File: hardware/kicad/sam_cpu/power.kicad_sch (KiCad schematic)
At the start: 29 parts, among them J11 J11 POWER, J17 EXT 5V, Q1 AO3401A, Q2 AO3401A, U1 LTC4412, U2 LTC4412, U3 AMS1117-3.3

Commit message: Redraw the schematic with wires (draft 0.2)
Every connection is now a wire, and each connector sits on the page of the
parts that drive or read it (Pi header with the RP2354B, J6/J12 with their
comparators and 74HC165, J1 with the 74HC595, J2/J3/J13 with their filters).
Signals between pages use global labels with page references. The Pi page is
merged into the MCU page; the Pi 4 sits on the 40-pin header J21.

ERC: 0 errors, 1 warning. Netlist check: 1266 pins, 299 nets, no differences.

Co-Authored-By: Claude Opus 5.5 (1M context) <noreply@anthropic.com>
Claude-Session: https://claude.ai/code/session_019DLTv1F2PjepjxqiUcAMKV
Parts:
- added C10: 100n, Capacitor_SMD:C_0603_1608Metric, symbol Device:C
- added D4: S1M, Diode_SMD:D_SMA, symbol Device:D
- C1: value 47u -> 100u; footprint Capacitor_SMD:CP_Elec_6.3x7.7 -> Capacitor_SMD:CP_Elec_8x10
- C3: value 100u -> 47u; footprint Capacitor_SMD:CP_Elec_8x10 -> Capacitor_SMD:CP_Elec_6.3x7.7
- C4: footprint Capacitor_SMD:CP_Elec_8x10 -> Capacitor_SMD:CP_Elec_6.3x7.7
- C8: value 100n -> 100u; footprint Capacitor_SMD:C_0603_1608Metric -> Capacitor_SMD:CP_Elec_6.3x7.7; symbol Device:C -> Device:C_Polarized
- FB1: value FB 3A -> 3A
- FB2, FB3: value FB 1A -> 1A
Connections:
- net +12V: now also C2.1; no longer C1.1
- net +5V: now also D4.2 (A)
- net -12V: now also C3.2; no longer C2.2
- net GND: now also C2.2, C3.1, C10.2; no longer C2.1, C3.2
- net VMON_12V: now also C10.1; no longer C9.1
- net VMON_5V: now also C9.1; no longer C8.1
- net +12V_IN: no longer names the net of FB2.1, J11.6 (Pin_6)
- net +5V_EXT: no longer names the net of D1.1 (A1), J17.1 (Pin_1), Q1.3 (D), R1.1, U1.1 (VIN)
- net +5V_EXT: now also C1.1; no longer C3.1
- net +5V_J11: no longer names the net of JP1.2 (B), Q2.3 (D), U2.1 (VIN)
- net +5V_J11_F: no longer names the net of FB1.2, JP1.1 (A)
- net +5V_J11_IN: no longer names the net of FB1.1, J11.1 (Pin_1)
- net -12V_IN: no longer names the net of FB3.1, J11.3 (Pin_3)
- net EXT_PRESENT: no longer names the net of R1.2, R2.1, U2.3 (CTL)
- net GATE_EXT: no longer names the net of Q1.1 (G), U1.5 (GATE)
- net GATE_J11: no longer names the net of Q2.1 (G), U2.5 (GATE)
- new net +4V5: C8.1, D4.1 (K)
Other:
- note added: "3.3 V"
- note added: "4.5 V for the switch matrix"
- note added: "External +5 V (J17, priority)"
- note added: "IO board power (J11)"
- note removed: "3.3 V regulator"
- note removed: "Ideal-diode power mux"
- note removed: "J11: power from the IO board (J16 harness)"
- note removed: "J17: external +5 V (priority)"
- title: Power: +5 V mux (external / J11), 3.3 V, supply monitors -> Power: +5 V mux (external / J11), 3.3 V, 4.5 V, supply monitors
- moved on the sheet: C1, C2, C3, C4, C5, C6, C7, C9, D1, D2, FB1, FB2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

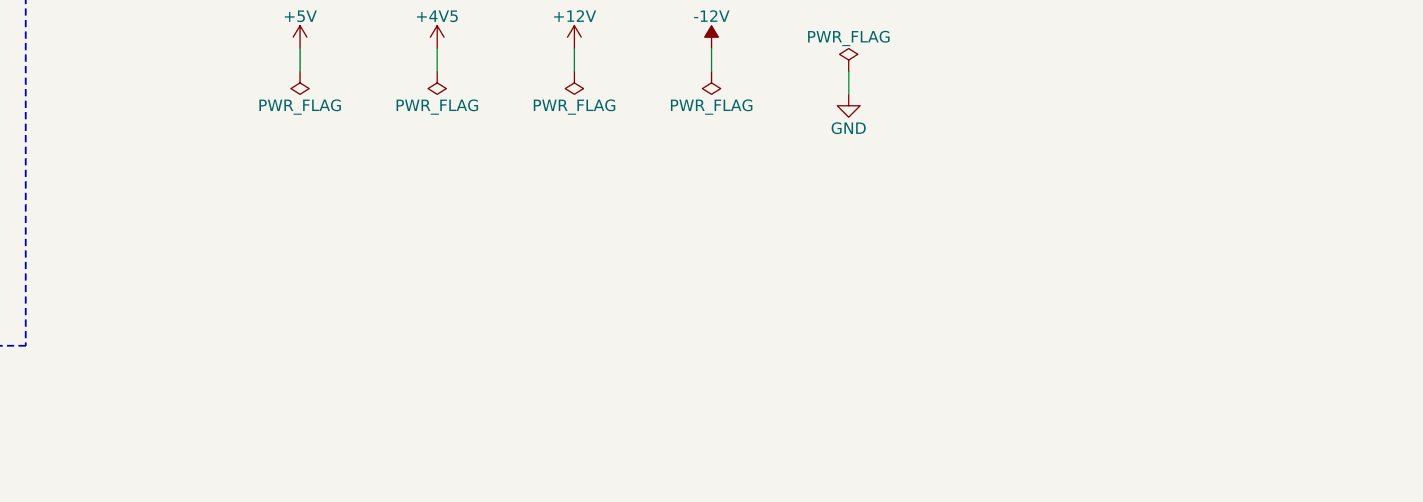
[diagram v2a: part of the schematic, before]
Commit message: Add RTC, test points and stereo speaker connector; place all parts on 2 layers
Schematic: DS3231MZ real-time clock on the Pi I2C1 with a CR2032 holder,
22 test points (rails, bus, strobes, switch chain, VREF, DAC outputs) and
J22, a second KK-396 speaker connector with L and R as separate pairs.
ERC 0 errors, generated netlist matches the intended nets.

PCB: 2 copper layers. The RP2354B sits near J9 with its USB-C on the top
edge 13 mm from the USB pins; decoupling, regulator and crystal parts on
their pins; every other part grouped by sheet next to its connector, low
parts only under the Pi. J17 and J22 on the right edge; Pi and J5 12 mm
lower to fit the audio parts.

Co-Authored-By: Claude Opus 5.5 (1M context) <noreply@anthropic.com>
Claude-Session: https://claude.ai/code/session_01ExuDVoDDDHhVWjb8EwVzYb
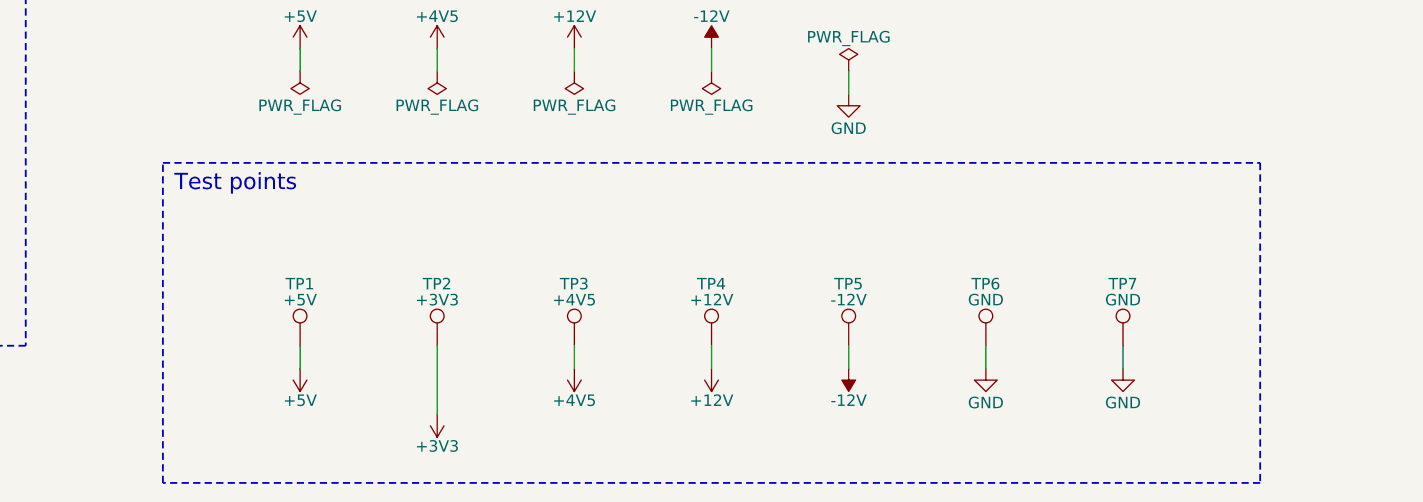
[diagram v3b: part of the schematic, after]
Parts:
- added TP1: +5V, TestPoint:TestPoint_Pad_D1.5mm, symbol Connector:TestPoint
- added TP2: +3V3, TestPoint:TestPoint_Pad_D1.5mm, symbol Connector:TestPoint
- added TP3: +4V5, TestPoint:TestPoint_Pad_D1.5mm, symbol Connector:TestPoint
- added TP4: +12V, TestPoint:TestPoint_Pad_D1.5mm, symbol Connector:TestPoint
- added TP5: -12V, TestPoint:TestPoint_Pad_D1.5mm, symbol Connector:TestPoint
- added TP6, TP7: GND, TestPoint:TestPoint_Pad_D1.5mm, symbol Connector:TestPoint
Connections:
- net +12V: now also TP4.1
- net +3V3: now also TP2.1
- net +4V5: now also TP3.1
- net +5V: now also TP1.1
- net -12V: now also TP5.1
- net GND: now also TP6.1, TP7.1
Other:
- note added: "Test points"

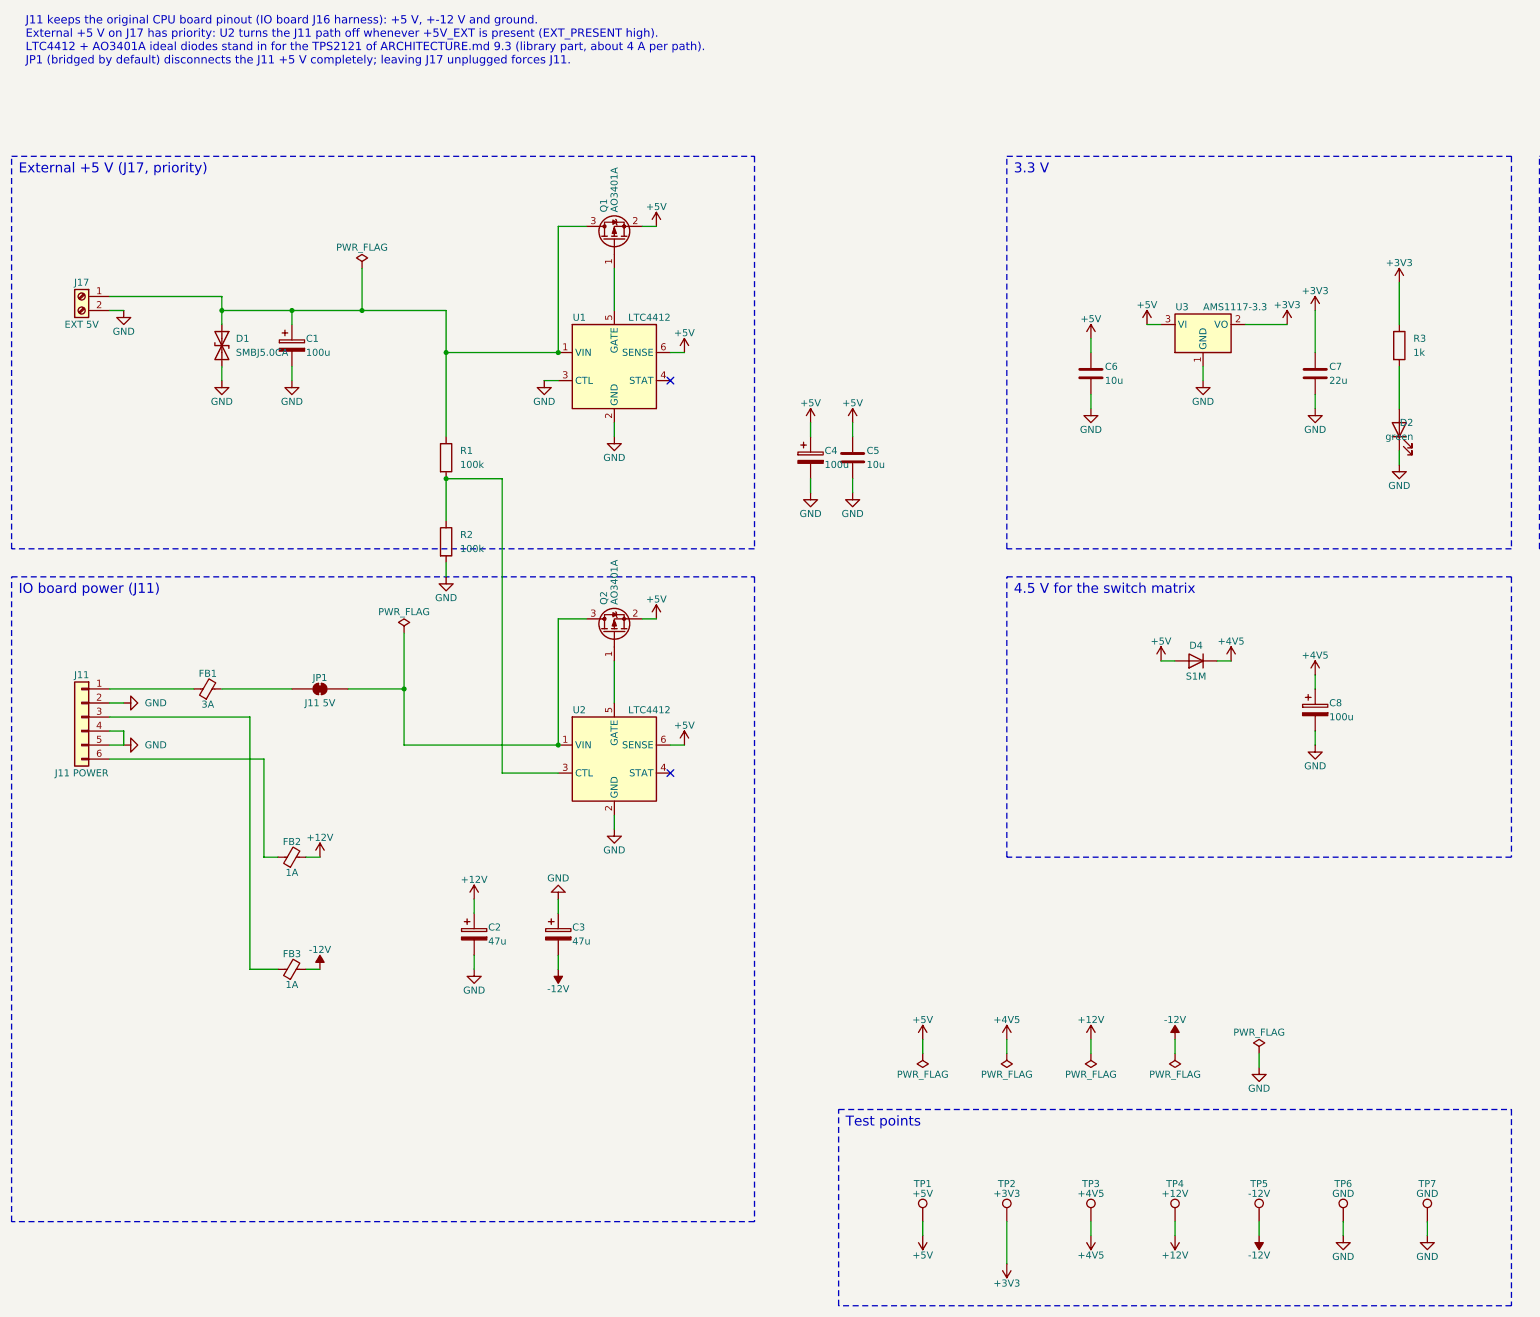
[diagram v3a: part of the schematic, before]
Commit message: Audio on external 12 V with TDA7297 stereo + subwoofer amps, NCP1117, guide regulator layout
- Remove the +-12 V input from J11; J23 external +12 V with polyfuse and TVS
- Replace the two TDA2030A with a TDA7297 bridge amp for left/right (J10, J22)
  and a second TDA7297 for the subwoofer (J24), fed by an (L+R)/2 110 Hz
  Sallen-Key low-pass (OPA1678); shared standby and RP2354B-controlled mute
- AMS1117 -> NCP1117-3.3 (ceramic-stable, as in the RP2350 guide), 10 uF 1206
- L1 and crystal part numbers from the RP2350 hardware guide
- Place the core regulator parts by hand following the Pico 2 layout; amps in a
  row with a heatsink keep-out; J23/J22/J24 on the right edge

Co-Authored-By: Claude Opus 5.5 (1M context) <noreply@anthropic.com>
Claude-Session: https://claude.ai/code/session_01ExuDVoDDDHhVWjb8EwVzYb
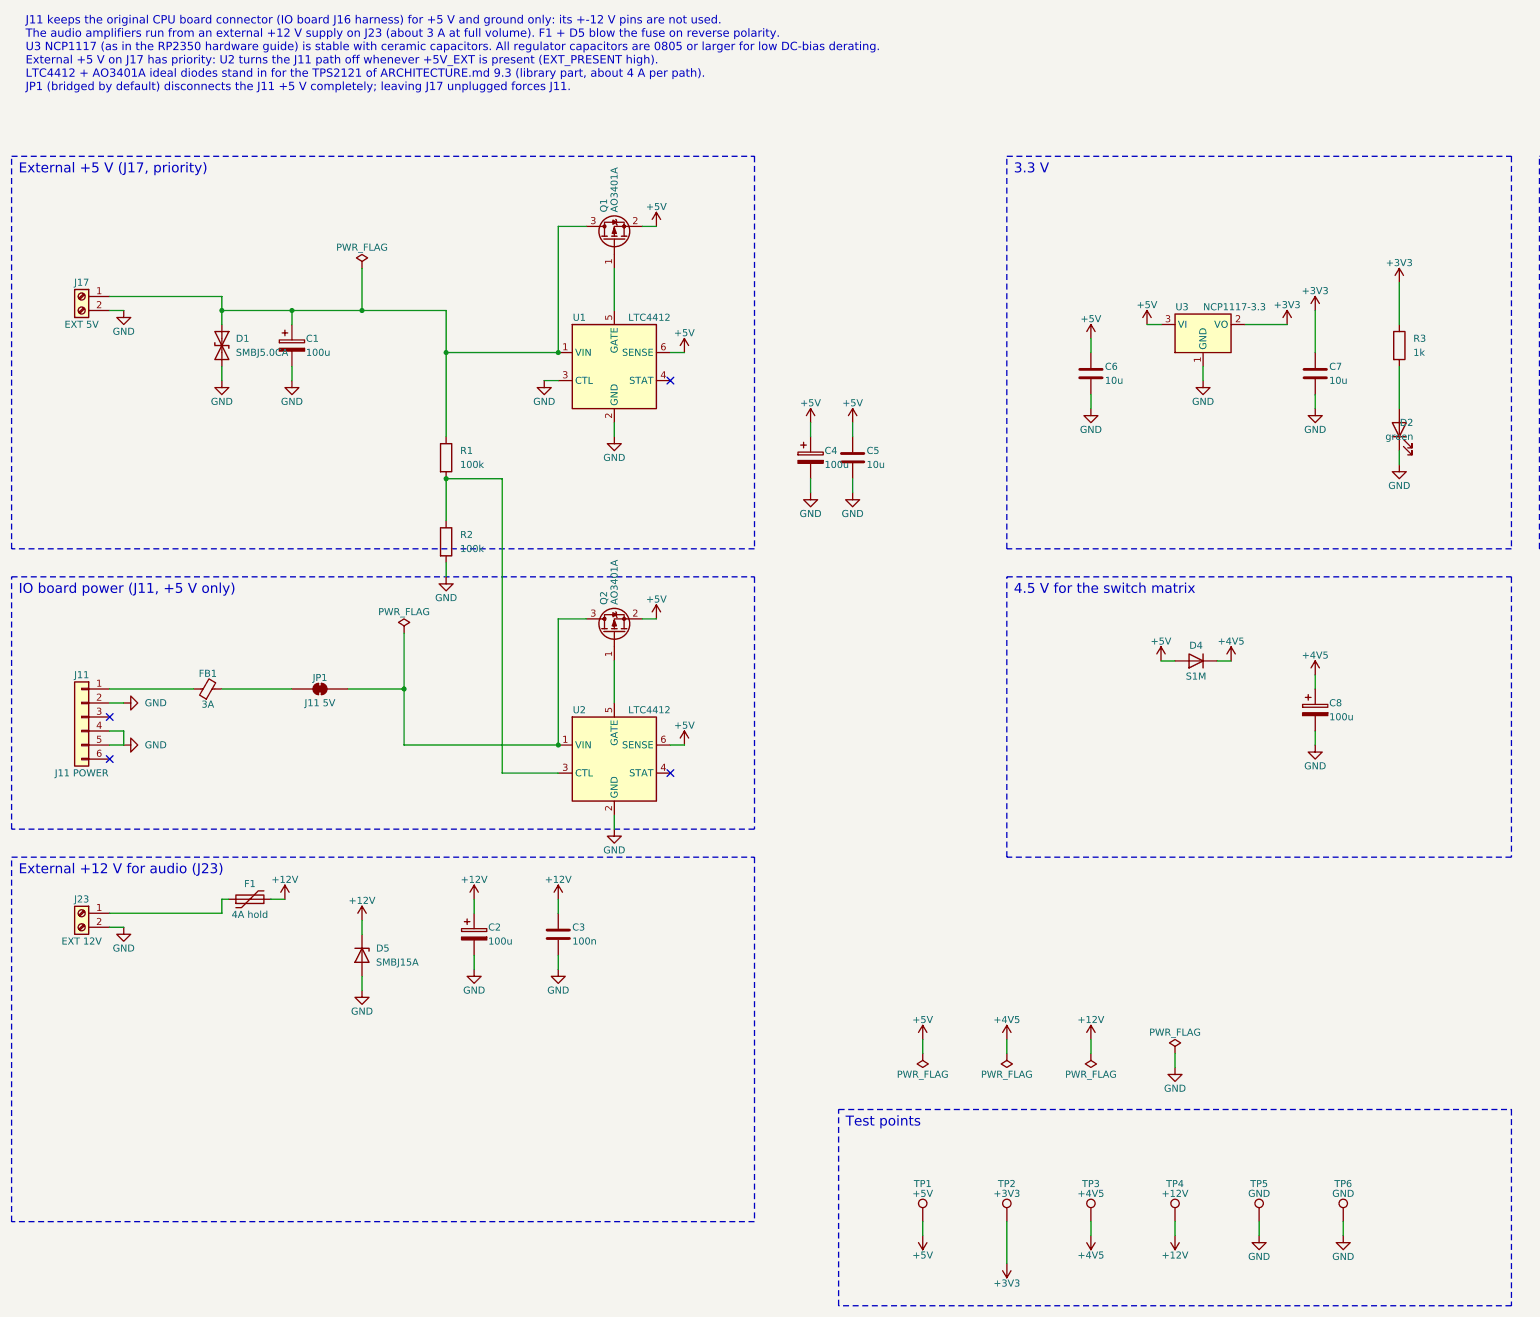
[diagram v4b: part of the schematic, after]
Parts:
- removed FB2, FB3: 1A, Inductor_SMD:L_0805_2012Metric, symbol Device:FerriteBead_Small
- removed TP7: GND, TestPoint:TestPoint_Pad_D1.5mm, symbol Connector:TestPoint
- added D5: SMBJ15A, Diode_SMD:D_SMB, symbol Device:D_Zener
- added F1: 4A hold, Fuse:Fuse_2920_7451Metric, symbol Device:Polyfuse
- added J23: EXT 12V, TerminalBlock_Phoenix:TerminalBlock_Phoenix_MKDS-1,5-2-5.08_1x02_P5.08mm_Horizontal, symbol Connector:Screw_Terminal_01x02
- C2: value 47u -> 100u; footprint Capacitor_SMD:CP_Elec_6.3x7.7 -> Capacitor_SMD:CP_Elec_8x10
- C3: value 47u -> 100n; footprint Capacitor_SMD:CP_Elec_6.3x7.7 -> Capacitor_SMD:C_0603_1608Metric; symbol Device:C_Polarized -> Device:C
- C6: footprint Capacitor_SMD:C_0805_2012Metric -> Capacitor_SMD:C_1206_3216Metric
- C7: value 22u -> 10u; footprint Capacitor_SMD:C_0805_2012Metric -> Capacitor_SMD:C_1206_3216Metric
- TP5: value -12V -> GND
- U3: value AMS1117-3.3 -> NCP1117-3.3; symbol Regulator_Linear:AMS1117-3.3 -> Regulator_Linear:NCP1117-3.3_SOT223
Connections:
- net -12V is gone; now on net GND: C3.2, TP5.1
- net +12V: now also C3.1, D5.1 (K), F1.2
- net GND: now also D5.2 (A), J23.2 (Pin_2); no longer C3.1
- new net: F1.1, J23.1 (Pin_1)
- no-connect marks 2 -> 4
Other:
- note added: "External +12 V for audio (J23)"
- note added: "IO board power (J11, +5 V only)"
- note added: "J11 keeps the original CPU board connector (IO board J16 harness) for +5 V and ground only: its +-12 V pins are not used. The audio amplifiers run from an external +12 V supply on J23 (about 3 A at full volume). F1 + D5 blow the fuse on reverse polarity. U3 NCP1117 (as in the RP2350 hardware guide) is stable with ceramic capacitors. All regulator capacitors are 0805 or larger for low DC-bias dera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"
- note removed: "IO board power (J11)"
- note removed: "J11 keeps the original CPU board pinout (IO board J16 harness): +5 V, +-12 V and ground. External +5 V on J17 has priority: U2 turns the J11 path off whenever +5V_EXT is present (EXT_PRESENT high). LTC4412 + AO3401A ideal diodes stand in for the TPS2121 of ARCHITECTURE.md 9.3 (library part, about 4 A per path). JP1 (bridged by default) disconnects the J11 +5 V completely; leaving J17 unplugged fo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"
- title: Power: +5 V mux (external / J11), 3.3 V, 4.5 V, supply monitors -> Power: +5 V mux, external +12 V, 3.3 V, 4.5 V, monitors

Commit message: Power mux: one TI TPS2117 replaces U1/U2 LTC4412 + Q1/Q2
c33 (schematic): U1 is a TPS2117 (SOT-583-8, C22399676) in priority mode,
external +5 V on VIN1, J11 on VIN2, R1 100k / R2 33k on PR1 (VIN1 kept
above about 4 V). U2, Q1, Q2 and the +5V PWR_FLAG go.
c34 (board): U1 in the old Q1/Q2 spot; R1 (now 0402) and R2 moved next to
it, PR1 crosses under U1 on B.Cu. EXT_5V / J11_5V join the Power_5V class.
Still 36 unconnected items, no new DRC errors, parity as before, ERC clean.

Co-Authored-By: Claude Opus 5.5 (1M context) <noreply@anthropic.com>
Claude-Session: https://claude.ai/code/session_01ExuDVoDDDHhVWjb8EwVzYb
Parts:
- removed Q1, Q2: AO3401A, Package_TO_SOT_SMD:SOT-23, symbol Transistor_FET:AO3401A
- removed U2: LTC4412, Package_TO_SOT_SMD:TSOT-23-6, symbol Power_Management:LTC4412xS6
- R1: footprint Resistor_SMD:R_0603_1608Metric -> Resistor_SMD:R_0402_1005Metric
- R2: value 100k -> 33k
- U1: value LTC4412 -> TPS2117; footprint Package_TO_SOT_SMD:TSOT-23-6 -> Package_TO_SOT_SMD:SOT-583-8; symbol Power_Management:LTC4412xS6 -> Power_Management:TPS2116DRL
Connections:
- net +5V: now also U1.2 (VOUT), U1.7 (VOUT); no longer U1.6 (SENSE)
- net GND: now also U1.1 (GND); no longer U1.2 (GND), U1.3 (CTL)
- net J11_5V: now reaches JP1.2 (B)
- net J11_5V: now also U1.6 (VIN2)
- net EXT_5V: now reaches C1.1, D1.1 (A1), J17.1 (Pin_1), R1.1
- net EXT_5V: now also U1.3 (VIN1), U1.5 (MODE); no longer U1.1 (VIN)
- net at R1.2, R2.1: now also U1.4 (PR1)
- no-connect marks 4 -> 3
